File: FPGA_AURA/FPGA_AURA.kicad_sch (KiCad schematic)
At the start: 0 parts

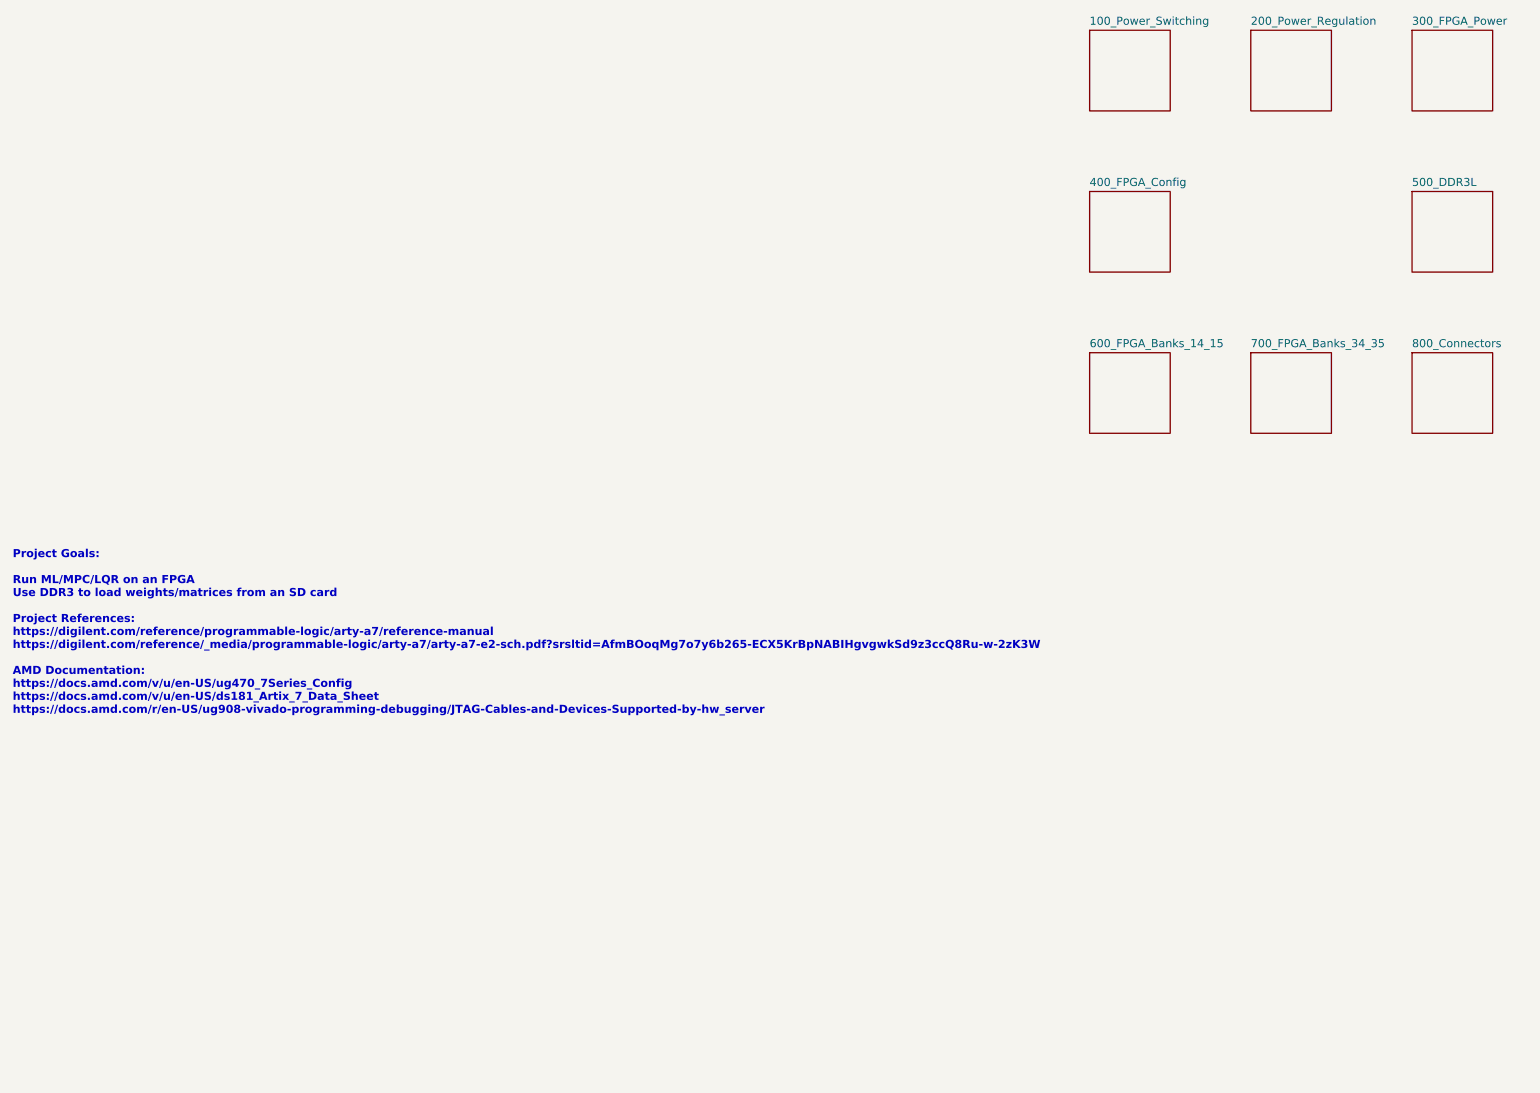
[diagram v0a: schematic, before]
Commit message: Following new DDR3 reference
Using Scopefun v2 as a reference design for the XC7A35T-FTG256
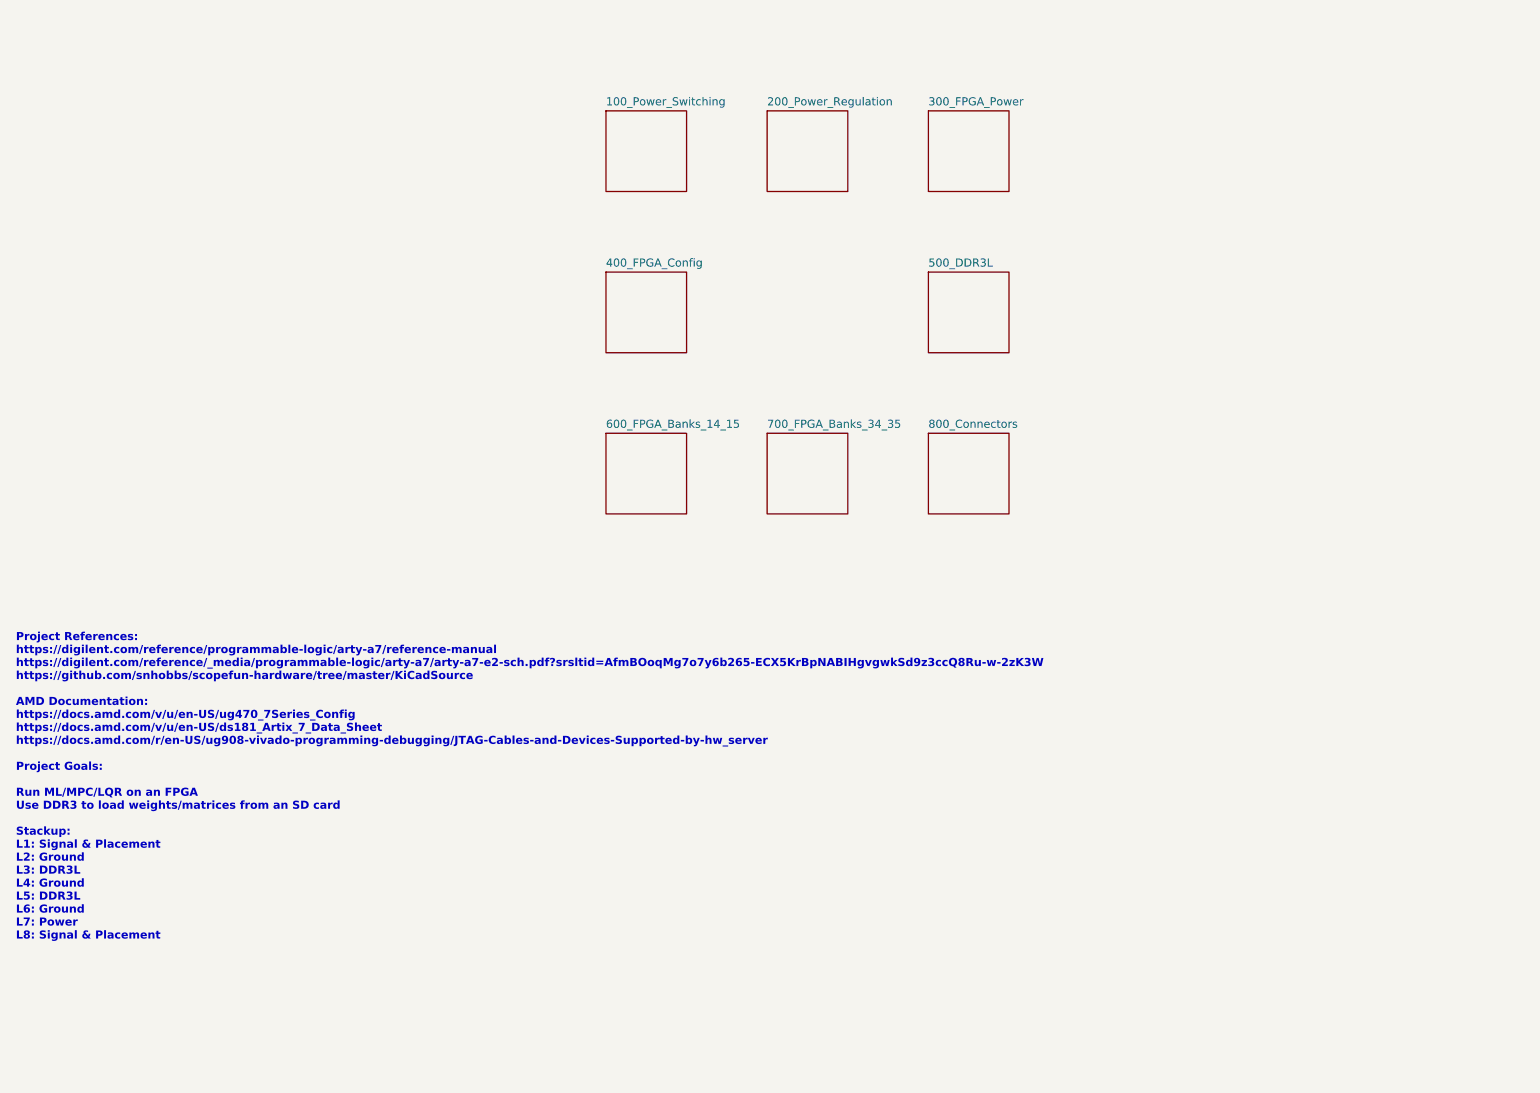
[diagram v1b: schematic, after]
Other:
- note added: "Project References: https://digilent.com/reference/programmable-logic/arty-a7/reference-manual https://digilent.com/reference/_media/programmable-logic/arty-a7/arty-a7-e2-sch.pdf?srsltid=AfmBOoqMg7o7y6b265-ECX5KrBpNABIHgvgwkSd9z3ccQ8Ru-w-2zK3W https://github.com/snhobbs/scopefun-hardware/tree/master/KiCadSource AMD Documentation: https://docs.amd.com/v/u/en-US/ug470_7Series_Config https://docs.am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"
- note removed: "Project Goals: Run ML/MPC/LQR on an FPGA Use DDR3 to load weights/matrices from an SD card Project References: https://digilent.com/reference/programmable-logic/arty-a7/reference-manual https://digilent.com/reference/_media/programmable-logic/arty-a7/arty-a7-e2-sch.pdf?srsltid=AfmBOoqMg7o7y6b265-ECX5KrBpNABIHgvgwkSd9z3ccQ8Ru-w-2zK3W AMD Documentation: https://docs.amd.com/v/u/en-US/ug470_7Series_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"
- company: (none) -> Alexander Armitage
- title: (none) -> FPGA AURA

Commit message: Moving to laptop
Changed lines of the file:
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@@
 		(company "Alexander Armitage")
 	)
-	(text "Project References:\nhttps://digilent.com/reference/programmable-logic/arty-a7/reference-manual\nhttps://digilent.com/reference/_media/programmable-logic/arty-a7/arty-a7-e2-sch.pdf?srsltid=AfmBOoqMg7o7y6b265-ECX5KrBpNABIHgvgwkSd9z3ccQ8Ru-w-2zK3W\nhttps://github.com/snhobbs/scopefun-hardware/tree/master/KiCadSource\n\nAMD Documentation:\nhttps://docs.amd.com/v/u/en-US/ug470_7Series_Config\nhttps://docs.amd.com/v/u/en-US/ds181_Artix_7_Data_Sheet\nhttps://docs.amd.com/r/en-US/ug908-vivado-programming-debugging/JTAG-Cables-and-Devices-Supported-by-hw_server\n\nProject Goals:\n\nRun ML/MPC/LQR on an FPGA\nUse DDR3 to load weights/matrices from an SD card\n\nStackup:\nL1: Signal & Placement\nL2: Ground\nL3: DDR3L\nL4: Ground\nL5: DDR3L\nL6: Ground\nL7: Power\nL8: Signal & Placement"
+	(text "Project References:\nhttps://digilent.com/reference/programmable-logic/arty-a7/reference-manual\nhttps://digilent.com/reference/_media/programmable-logic/arty-a7/arty-a7-e2-sch.pdf?srsltid=AfmBOoqMg7o7y6b265-ECX5KrBpNABIHgvgwkSd9z3ccQ8Ru-w-2zK3W\nhttps://github.com/snhobbs/scopefun-hardware/tree/master/KiCadSource\n\nAMD Documentation:\nhttps://docs.amd.com/v/u/en-US/ug470_7Series_Config\nhttps://docs.amd.com/v/u/en-US/ds181_Artix_7_Data_Sheet\nhttps://docs.amd.com/r/en-US/ug583-ultrascale-pcb-design/DDR3-SDRAM-Interface-Signal-Description\nhttps://docs.amd.com/r/en-US/ug908-vivado-programming-debugging/JTAG-Cables-and-Devices-Supported-by-hw_server\n\nProject Goals:\n\nRun ML/MPC/LQR on an FPGA\nUse DDR3 to load weights/matrices from an SD card\n\nStackup:\nL1: Signal & Placement\nL2: Ground\nL3: DDR3L\nL4: Ground\nL5: DDR3L\nL6: Ground\nL7: Power\nL8: Signal & Placement"
 		(exclude_from_sim no)
 		(at 21.336 168.91 0)

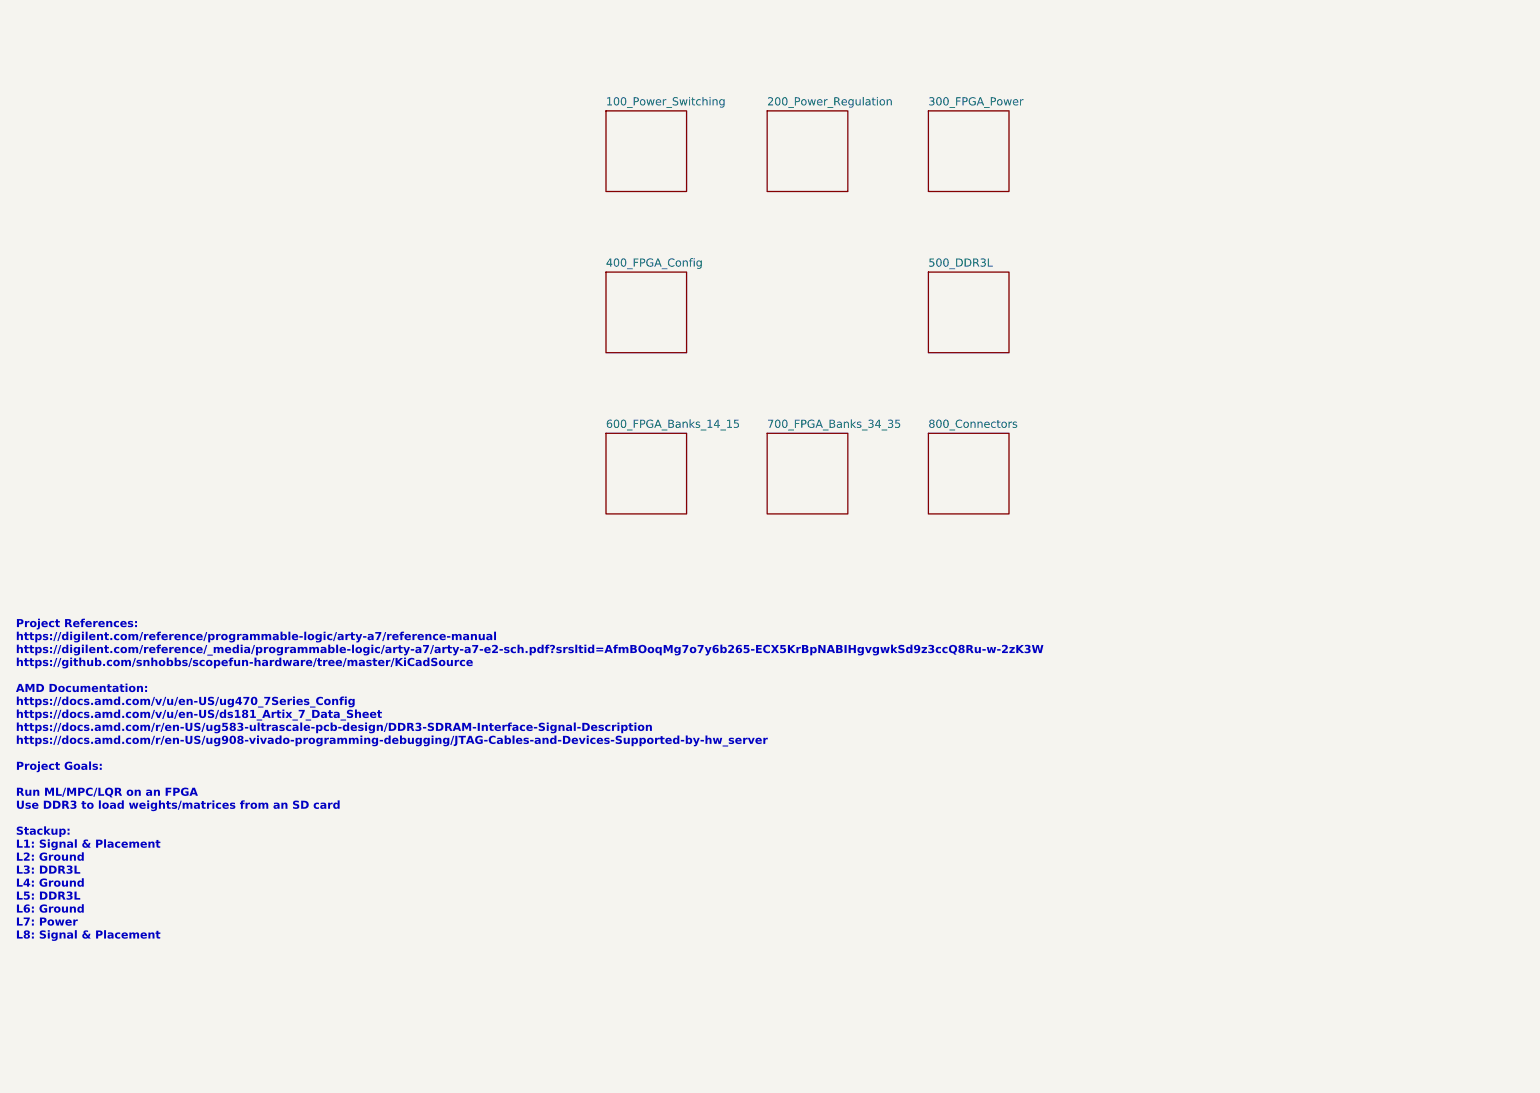
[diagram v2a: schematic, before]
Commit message: Moved to KiCAD V10 for delay.
The FPGA PCB has now been moved to KiCAD V10 to make use of the new delay features and design rules are being setup.

PCB stack-up has now been decided.
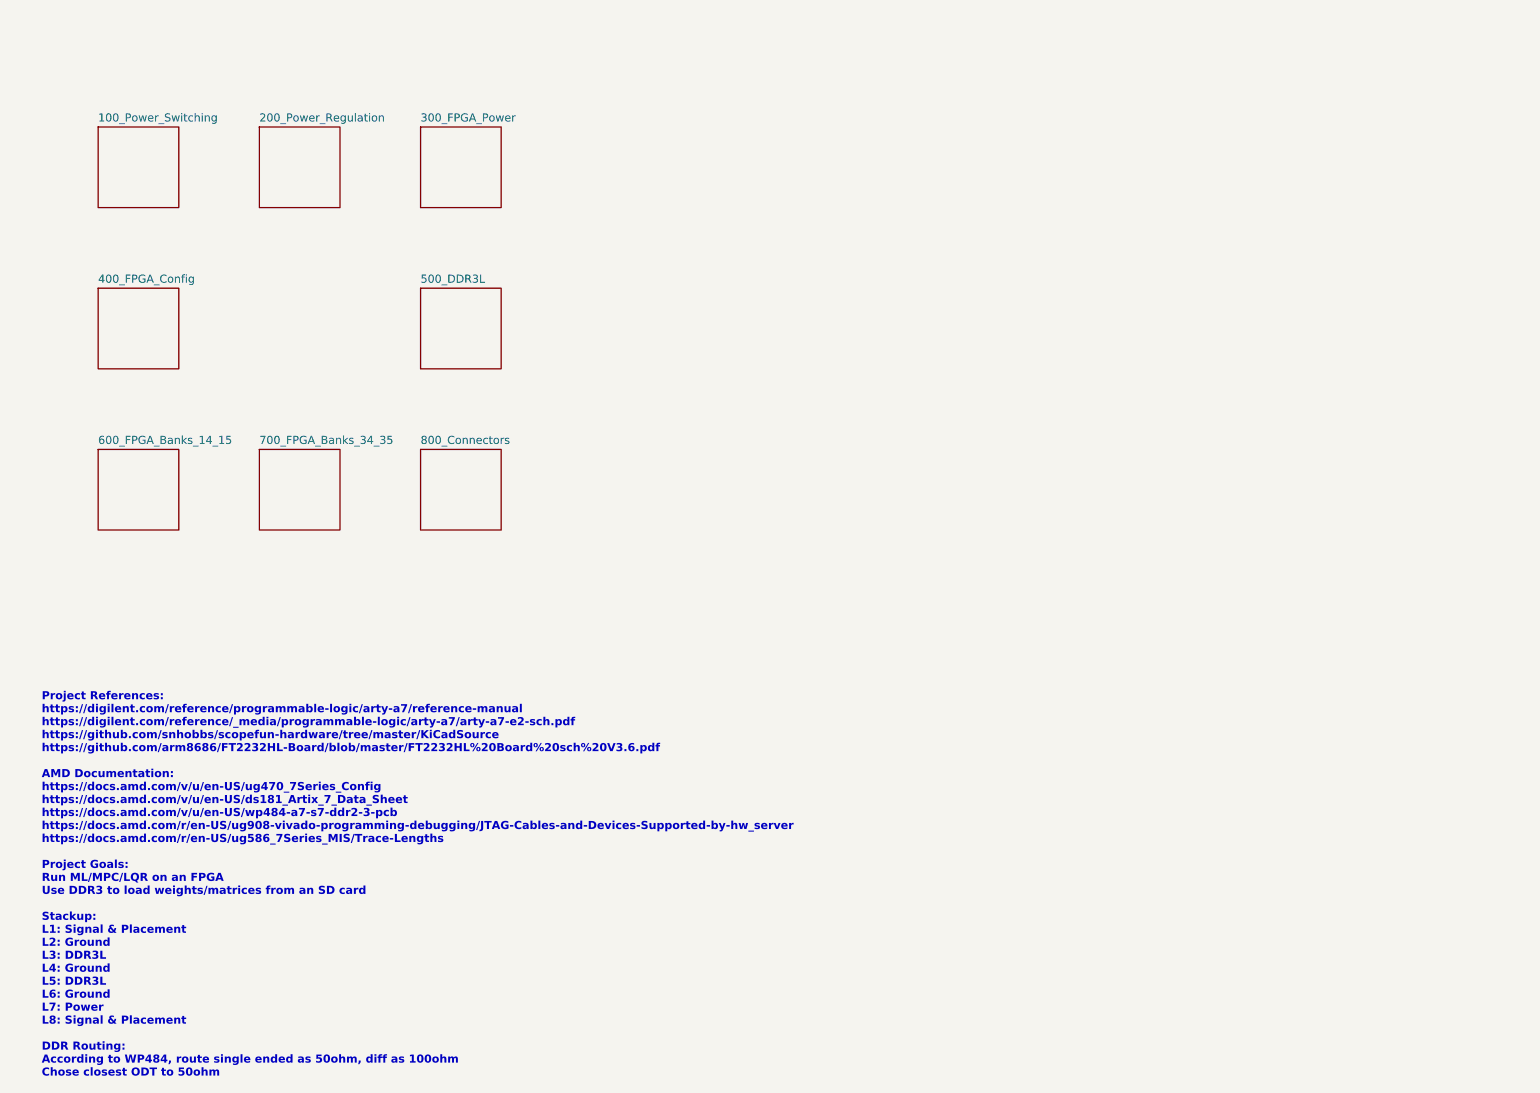
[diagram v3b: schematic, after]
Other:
- note added: "Project References: https://digilent.com/reference/programmable-logic/arty-a7/reference-manual https://digilent.com/reference/_media/programmable-logic/arty-a7/arty-a7-e2-sch.pdf https://github.com/snhobbs/scopefun-hardware/tree/master/KiCadSource https://github.com/arm8686/FT2232HL-Board/blob/master/FT2232HL%20Board%20sch%20V3.6.pdf AMD Documentation: https://docs.amd.com/v/u/en-US/ug470_7Series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"
- note removed: "Project References: https://digilent.com/reference/programmable-logic/arty-a7/reference-manual https://digilent.com/reference/_media/programmable-logic/arty-a7/arty-a7-e2-sch.pdf?srsltid=AfmBOoqMg7o7y6b265-ECX5KrBpNABIHgvgwkSd9z3ccQ8Ru-w-2zK3W https://github.com/snhobbs/scopefun-hardware/tree/master/KiCadSource AMD Documentation: https://docs.amd.com/v/u/en-US/ug470_7Series_Config https://docs.am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"
